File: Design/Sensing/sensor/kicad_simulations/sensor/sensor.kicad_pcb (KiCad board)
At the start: 2 copper layers, 44 parts, among them J1 Conn_02x14_Counter_Clockwise, J11 Conn_01x01_Pin, J12 Conn_01x02_Pin, J15 Conn_01x02_Pin, J16 Conn_01x01_Pin, J17 Conn_01x02_Pin, J18 Conn_01x01_Pin, J4 Conn_01x02_Pin, J6 Conn_01x01_Pin, J7 Conn_01x02_Pin, J9 Conn_01x02_Pin, Q1 MMBT2222A, Q2 MMBT2222A, Q3 MMBT2222A, U1 TSSP58038, U2 TSSP58038, U3 TSSP58038, U4 BUF602xD, U5 BUF602xD, U6 BUF602xD

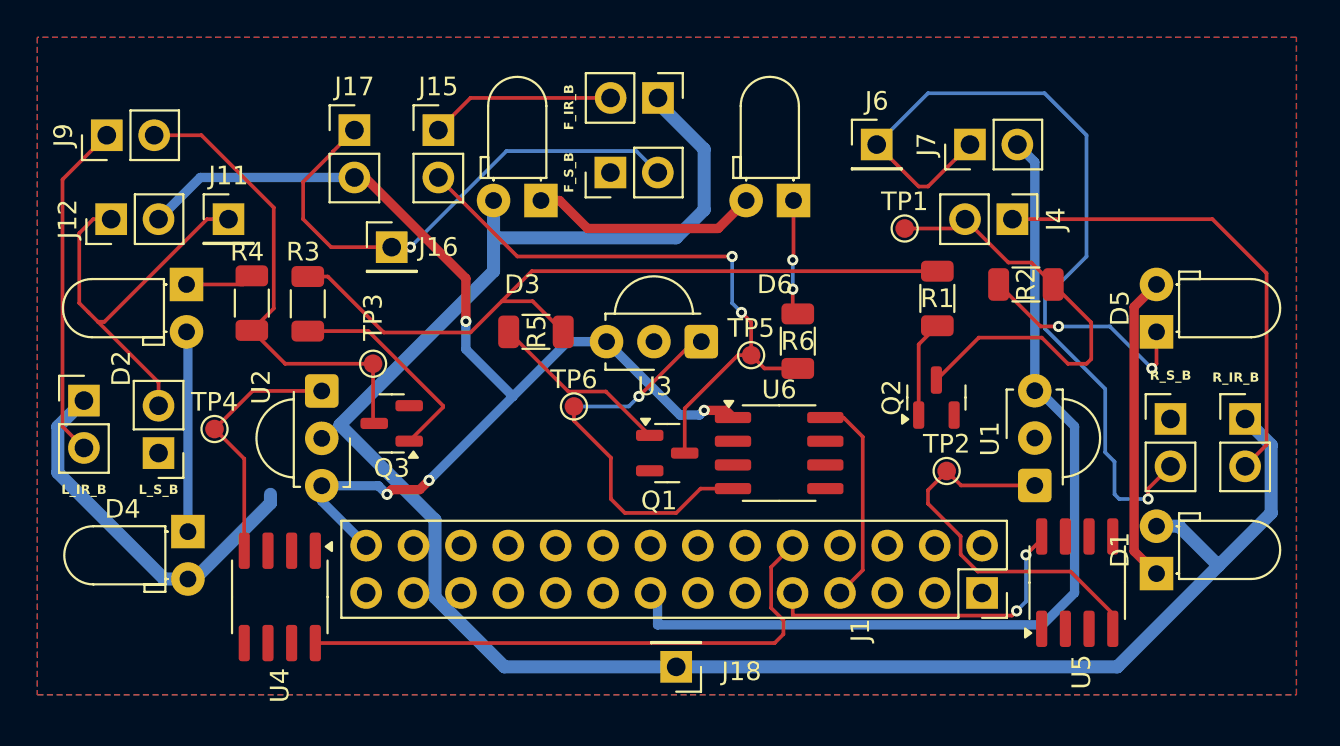
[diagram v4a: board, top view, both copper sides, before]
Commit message: Only two unrouted and 3 errors remaining
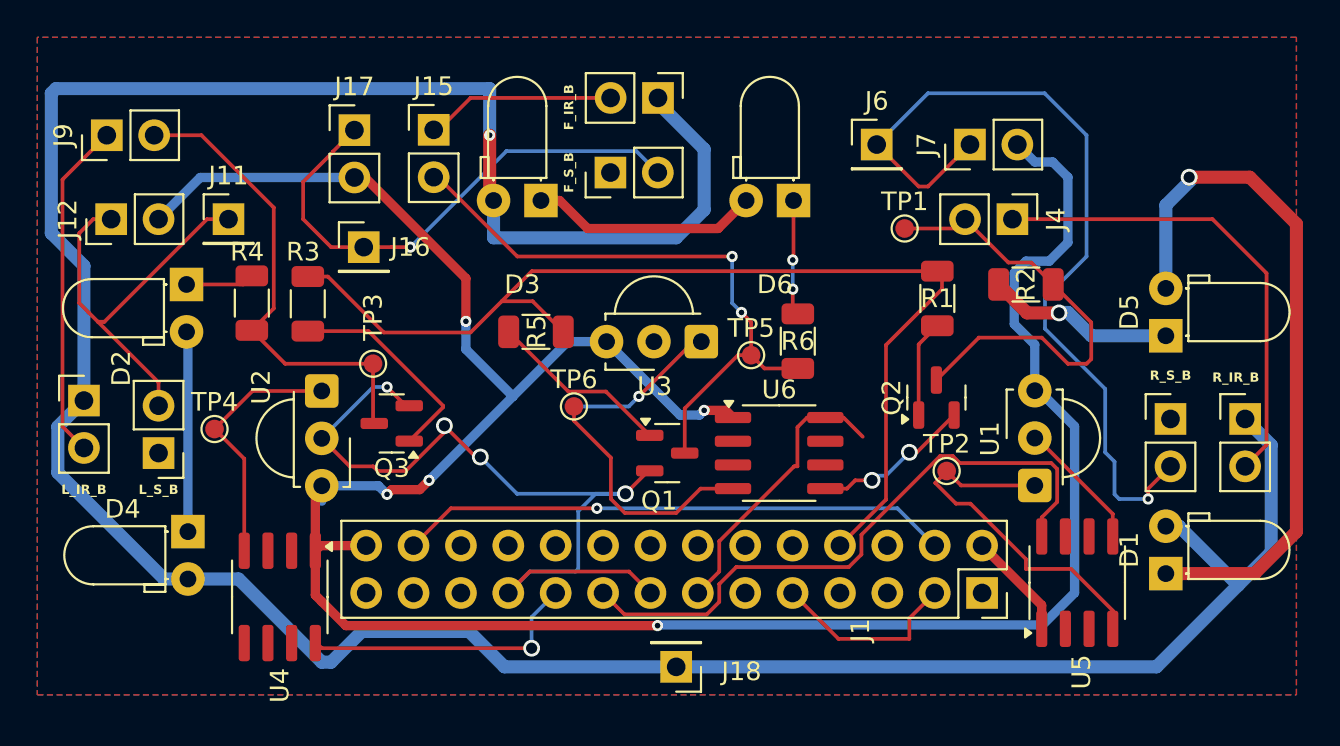
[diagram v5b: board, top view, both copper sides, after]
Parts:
- moved J16 1.50 mm to (101.5, 104.5)
- moved D5 0.54 mm to (144.5, 109.2)
- moved D1 0.50 mm to (144.5, 122.0)
- moved J15 0.25 mm to (105.2, 98.2)
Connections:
- J1 pad 10: /PC4 -> /PE14
- J1 pad 11: GND -> /PA5
- J1 pad 12: /PC5 -> /PA13
- J1 pad 13: /AB0 -> /PA6
- J1 pad 14: GND -> /PE12
- J1 pad 15: /3V3 -> GND
- J1 pad 16: /BATT -> /PE11
- J1 pad 17: /RESV2 -> /PA7
- J1 pad 18: /PE15 -> /PA10
- J1 pad 19: /PE14 -> /PC4
- J1 pad 2: GND -> /3V3
- J1 pad 20: /PA13 -> /PE9
- J1 pad 21: /PE12 -> GND
- J1 pad 22: /PE11 -> /PE8
- J1 pad 23: /5V -> /PC5
- J1 pad 24: /PE9 -> /RESV1
- J1 pad 25: /5V -> /AB0
- J1 pad 26: /5V -> /BATT
- J1 pad 27: /BATT -> GND
- J1 pad 3: /PA3 -> GND
- J1 pad 4: /PA4 -> /BATT
- J1 pad 5: GND -> /PA3
- J1 pad 6: /PA5 -> /RESV2
- J1 pad 7: /PA6 -> /PA4
- J1 pad 8: GND -> /PE15
- J1 pad 9: /PA7 -> GND
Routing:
- net GND: track 0.00 -> 72.6 mm, vias 0 -> 6
- net /5V: track 125.7 -> 159.0 mm, vias 0 -> 1
- net /3V3: track 109.1 -> 141.2 mm, vias 4 -> 5
- net /BATT: track 0.00 -> 29.6 mm, vias 0 -> 1
- net Net-(D1-K): track 16.5 -> 38.0 mm, vias 0 -> 1
- net /PE15: track 40.3 -> 57.4 mm
- net /PA7: track 17.9 -> 33.8 mm, vias 2 -> 0
- net /PC4: track 30.8 -> 15.2 mm, vias 0 -> 1
- net /PA6: track 11.3 -> 15.3 mm
- net Net-(D5-K): track 12.1 -> 10.1 mm, vias 2 -> 1
- net Net-(U1-OUT): track 20.9 -> 19.6 mm
- net Net-(J14-Pin_2): track 9.95 -> 10.5 mm

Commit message: pcb placement redo
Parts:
- removed F_IR_B, F_S_B, L_IR_B, L_S_B, R_IR_B, R_S_B: Conn_01x02_Pin, Connector_PinHeader_2.54mm:PinHeader_1x02_P2.54mm_Vertical
- removed J18: Conn_01x01_Pin, Connector_PinHeader_2.54mm:PinHeader_1x01_P2.54mm_Vertical
- removed U5, U6: BUF602xD, Package_SO:SOIC-8_3.9x4.9mm_P1.27mm
- added J10: Conn_01x02_Pin, Connector_PinHeader_2.54mm:PinHeader_1x02_P2.54mm_Vertical, F.Cu at (113.5, 94.0)
- added J13: Conn_01x02_Pin, Connector_PinHeader_2.54mm:PinHeader_1x02_P2.54mm_Vertical, F.Cu at (113.6, 98.5)
- added J14: Conn_01x01_Pin, Connector_PinHeader_2.54mm:PinHeader_1x01_P2.54mm_Vertical, F.Cu at (141.0, 126.0)
- added J2: Conn_01x02_Pin, Connector_PinHeader_2.54mm:PinHeader_1x02_P2.54mm_Vertical, F.Cu at (86.5, 123.0)
- added J3: Conn_02x14_Counter_Clockwise, Connector_PinSocket_2.54mm:PinSocket_2x14_P2.54mm_Vertical, F.Cu at (100.3, 121.8)
- added J5: L_S_B, Connector_PinHeader_2.54mm:PinHeader_1x02_P2.54mm_Vertical, F.Cu at (90.7, 110.7)
- added J8: Conn_01x02_Pin, Connector_PinHeader_2.54mm:PinHeader_1x02_P2.54mm_Vertical, F.Cu at (149.3, 112.3)
- J1: value Conn_02x14_Counter_Clockwise -> Conn_01x02_Pin; footprint Connector_PinSocket_2.54mm:PinSocket_2x14_P2.54mm_Vertical -> Connector_PinHeader_2.54mm:PinHeader_1x02_P2.54mm_Vertical
- J11, J16: value Conn_01x01_Pin -> Conn_01x02_Pin; footprint Connector_PinHeader_2.54mm:PinHeader_1x01_P2.54mm_Vertical -> Connector_PinHeader_2.54mm:PinHeader_1x02_P2.54mm_Vertical
- J15, J4: value Conn_01x02_Pin -> Conn_01x01_Pin; footprint Connector_PinHeader_2.54mm:PinHeader_1x02_P2.54mm_Vertical -> Connector_PinHeader_2.54mm:PinHeader_1x01_P2.54mm_Vertical
- Q1, Q2, Q3: value MMBT2222A -> MMBT5551L
- R4: value 18 -> 2.7k
- R5: value 2.7k -> 18
- U1: value TSSP58038 -> LM324; footprint OptoDevice:Vishay_MINICAST-3Pin -> Package_SO:SOIC-14_3.9x8.7mm_P1.27mm
- U4: value BUF602xD -> TSSP58038; footprint Package_SO:SOIC-8_3.9x4.9mm_P1.27mm -> OptoDevice:Vishay_MINICAST-3Pin
- moved J9 65.1 mm to (148.0, 123.0), turned to -90 degrees
- moved J12 57.5 mm to (144.7, 112.3), turned to 180 degrees
- moved J7 55.2 mm to (86.5, 127.0)
- moved D1 54.2 mm to (90.6, 116.7), turned to -90 degrees
- moved D4 52.1 mm to (144.2, 119.2), turned to 90 degrees
- moved J16 51.5 mm to (148.0, 126.7), turned to -90 degrees
- moved TP4 49.9 mm to (141.2, 99.5), turned to 90 degrees
- moved J1 48.9 mm to (86.7, 113.3), turned to 180 degrees
- moved J6 45.6 mm to (93.0, 127.0), turned to -90 degrees
- moved R1 41.0 mm to (94.0, 122.0), turned to 0 degrees
- moved R2 40.0 mm to (97.0, 106.0)
- moved D5 37.7 mm to (108.2, 98.8), turned to 180 degrees
- moved TP3 36.1 mm to (137.0, 119.3)
- moved D3 33.4 mm to (144.2, 106.2), turned to 90 degrees
- moved R5 32.9 mm to (141.0, 122.0)
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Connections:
- D2 pad 2: Net-(D2-A) -> Net-(D1-K)
- D4 pad 1: Net-(D2-A) -> Net-(D4-K)
- D4 pad 2: /5V -> Net-(D3-K)
- D5 pad 2: Net-(D1-K) -> /5V
- D6 pad 2: Net-(D3-K) -> Net-(D5-K)
- J1 pad 1: /RESV3 -> /5V
- J1 pad 2: /3V3 -> Net-(J1-Pin_2)
- J12 pad 1: Net-(J10-Pin_2) -> GND
- J12 pad 2: /3V3 -> Net-(J12-Pin_2)
- J15 pad 1: Net-(J14-Pin_2) -> Net-(J13-Pin_2)
- J16 pad 1: Net-(J13-Pin_2) -> Net-(J12-Pin_2)
- J4 pad 1: Net-(J3-Pin_2) -> /5V
- Q1 pad 3: Net-(J15-Pin_2) -> Net-(J2-Pin_2)
- Q2 pad 3: Net-(J4-Pin_2) -> Net-(J9-Pin_2)
- Q3 pad 3: Net-(J9-Pin_2) -> Net-(J11-Pin_2)
- R1 pad 1: Net-(Q2-B) -> Net-(Q1-B)
- R2 pad 1: Net-(J4-Pin_2) -> Net-(J2-Pin_2)
- R2 pad 2: Net-(D5-K) -> Net-(D2-K)
- R3 pad 1: Net-(Q3-B) -> Net-(Q2-B)
- R4 pad 1: Net-(J9-Pin_2) -> Net-(Q3-B)
- R4 pad 2: Net-(D2-K) -> /PE15
- R5 pad 1: Net-(Q1-B) -> Net-(J9-Pin_2)
- R5 pad 2: /PE15 -> Net-(D4-K)
- R6 pad 1: Net-(J15-Pin_2) -> Net-(J11-Pin_2)
- TP1 pad 1: Net-(J4-Pin_2) -> Net-(J2-Pin_2)
- TP2 pad 1: Net-(U1-OUT) -> Net-(U1A-+)
- TP4 pad 1: Net-(U2-OUT) -> Net-(J11-Pin_2)
- TP5 pad 1: Net-(J15-Pin_2) -> Net-(U1B-+)
- TP6 pad 1: Net-(U3-OUT) -> Net-(U1C-+)
- U1 pad 1: Net-(U1-OUT) -> /PC4
- U1 pad 2: GND -> /PC4
- U1 pad 3: /3V3 -> Net-(U1A-+)
- U2 pad 1: Net-(U2-OUT) -> Net-(U1A-+)
- U3 pad 1: Net-(U3-OUT) -> Net-(U1B-+)
- U4 pad 1: /3V3 -> Net-(U1C-+)
- U4 pad 2: unconnected-(U4-NC-Pad2) -> GND
- U4 pad 3: unconnected-(U4-NC-Pad3) -> /3V3
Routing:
- net /5V: track 159.0 -> 0.00 mm, vias 1 -> 0
- net /3V3: track 141.2 -> 0.00 mm, vias 5 -> 0
- net GND: track 72.6 -> 0.00 mm, vias 6 -> 0
- net /PE15: track 57.4 -> 0.00 mm
- net Net-(J5-Pin_2): track 46.1 -> 0.00 mm, vias 1 -> 0
- net Net-(D1-K): track 38.0 -> 0.00 mm, vias 1 -> 0
- net /PA7: track 33.8 -> 0.00 mm
- net Net-(J15-Pin_2): track 33.4 -> 0.00 mm, vias 2 -> 0
- net /BATT: track 29.6 -> 0.00 mm, vias 1 -> 0
- net Net-(J13-Pin_2): track 28.2 -> 0.00 mm, vias 1 -> 0
- net Net-(J3-Pin_2): track 25.7 -> 0.00 mm
- net Net-(J9-Pin_2): track 25.6 -> 0.00 mm
- net Net-(J4-Pin_2): track 24.4 -> 0.00 mm
- net Net-(J10-Pin_2): track 22.3 -> 0.00 mm
- net Net-(U3-OUT): track 21.4 -> 0.00 mm, vias 1 -> 0
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
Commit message: Routed correct design
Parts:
- removed D2, D4, D6: TSAL4400, LED_THT:LED_D3.0mm_Horizontal_O1.27mm_Z2.0mm_IRBlack
- removed J4: Conn_01x01_Pin, Connector_PinHeader_2.54mm:PinHeader_1x01_P2.54mm_Vertical
- R2, R5, R6: value 18 -> 22
- moved J11 51.5 mm to (146.0, 80.8), turned to 90 degrees
- moved R4 47.4 mm to (149.2, 94.0), turned to -90 degrees
- moved J14 41.0 mm to (166.0, 93.5), turned to 0 degrees
- moved Q3 40.9 mm to (148.5, 88.9)
- moved TP3 40.7 mm to (169.0, 94.0), turned to 0 degrees
- moved D1 38.9 mm to (119.8, 91.1), turned to -135 degrees
- moved J1 38.9 mm to (113.4, 85.0), turned to -45 degrees
- moved J7 38.6 mm to (114.0, 100.0), turned to -90 degrees
- moved J6 37.0 mm to (117.8, 99.5), turned to 90 degrees
- moved Q2 36.2 mm to (167.0, 105.5), turned to 90 degrees
- moved J5 35.8 mm to (122.1, 93.4), turned to -45 degrees
- moved D5 35.0 mm to (140.8, 85.8)
- moved R2 33.9 mm to (126.5, 89.2), turned to 90 degrees
- moved J8 32.7 mm to (165.7, 84.0), turned to 45 degrees
- moved J10 32.5 mm to (141.0, 76.8), turned to -90 degrees
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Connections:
- D1 pad 2: /5V -> /3V3
- D3 pad 2: /5V -> /3V3
- D5 pad 2: /5V -> /3V3
- J1 pad 1: /5V -> /3V3
- J10 pad 1: /5V -> /3V3
- J8 pad 1: /5V -> /3V3
- R2 pad 2: Net-(D2-K) -> Net-(D1-K)
- R5 pad 2: Net-(D4-K) -> Net-(D3-K)
- R6 pad 2: Net-(D6-K) -> Net-(D5-K)
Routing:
- net /3V3: track 0.00 -> 211.0 mm, vias 0 -> 2
- net GND: track 0.00 -> 98.7 mm, vias 0 -> 3
- net /PE15: track 0.00 -> 75.6 mm, vias 0 -> 3
- net Net-(J2-Pin_2): track 0.00 -> 30.2 mm
- net Net-(J1-Pin_2): track 0.00 -> 22.9 mm
- net Net-(U1B-+): track 0.00 -> 21.5 mm, vias 0 -> 2
- net Net-(J13-Pin_2): track 0.00 -> 20.9 mm, vias 0 -> 2
- net /PC4: track 0.00 -> 19.5 mm, vias 0 -> 1
- net Net-(J9-Pin_2): track 0.00 -> 19.3 mm, vias 0 -> 2
- net Net-(U1A-+): track 0.00 -> 19.2 mm, vias 0 -> 2
- net Net-(J11-Pin_2): track 0.00 -> 18.2 mm, vias 0 -> 2
- net /BATT: track 0.00 -> 16.3 mm
- net Net-(J8-Pin_2): track 0.00 -> 16.0 mm
- net Net-(J12-Pin_2): track 0.00 -> 14.8 mm
- net /PA6: track 0.00 -> 14.1 mm, vias 0 -> 1
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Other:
- board outline added: 61.2 x 37.5 mm
